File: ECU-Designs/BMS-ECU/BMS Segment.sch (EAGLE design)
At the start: 108 parts, among them Q1 P-CHANNEL_MOSFET_DMP3099L-7, Q10 P-CHANNEL_MOSFET_DMP3099L-7, Q11 P-CHANNEL_MOSFET_DMP3099L-7, Q12 P-CHANNEL_MOSFET_DMP3099L-7, Q13 NPN_BCP56T1, Q2 P-CHANNEL_MOSFET_DMP3099L-7, Q3 P-CHANNEL_MOSFET_DMP3099L-7, Q4 P-CHANNEL_MOSFET_DMP3099L-7, Q5 P-CHANNEL_MOSFET_DMP3099L-7, Q6 P-CHANNEL_MOSFET_DMP3099L-7, Q7 P-CHANNEL_MOSFET_DMP3099L-7, Q8 P-CHANNEL_MOSFET_DMP3099L-7, Q9 P-CHANNEL_MOSFET_DMP3099L-7

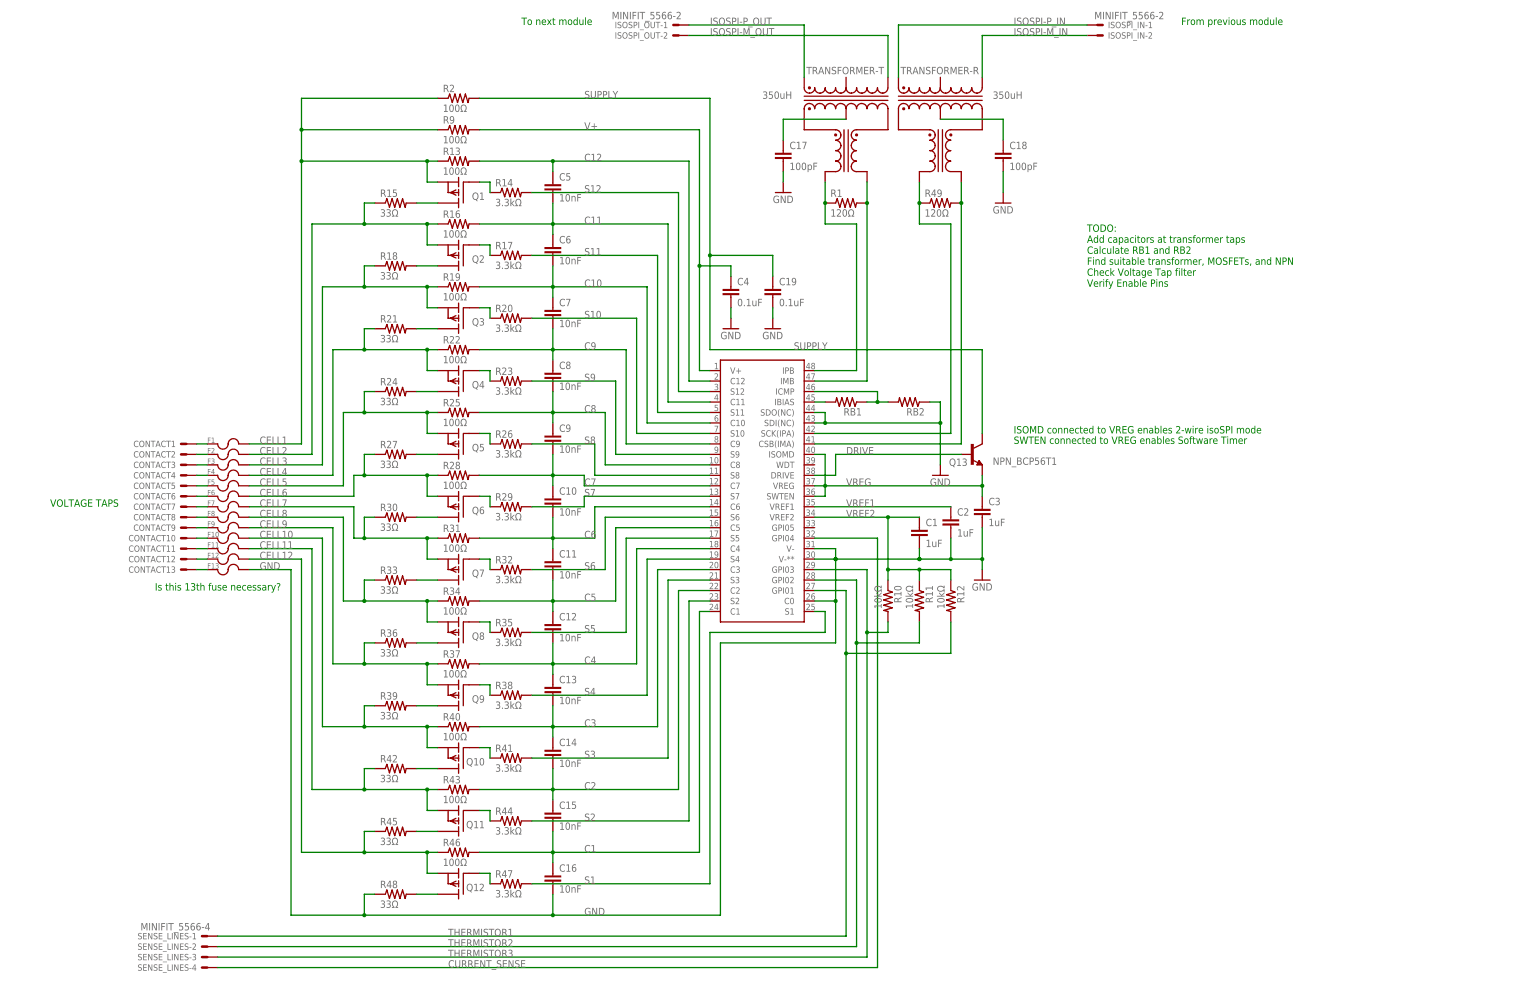
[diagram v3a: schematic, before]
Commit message: Update MC34161 name/desc, new 2016 vehicle pedal/dash controller board design, BSPD breakout test board
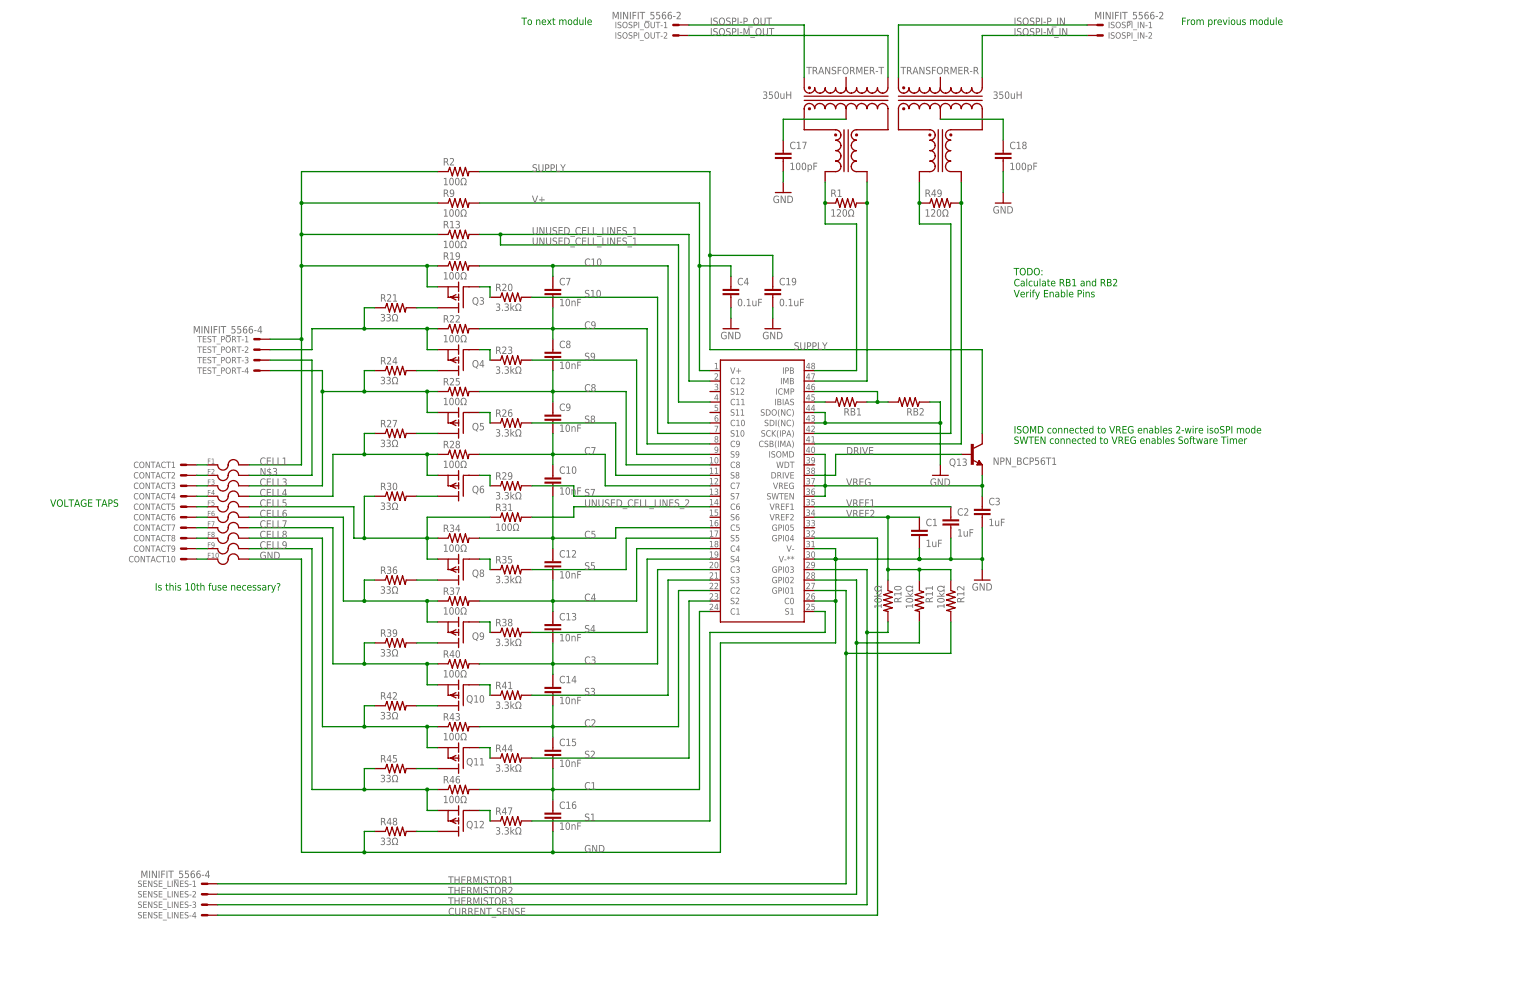
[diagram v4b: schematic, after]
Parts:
- removed C11, C5, C6: 10nF, HyTechDevices:CAP0805
- removed CONTACT11, CONTACT12, CONTACT13: SPRING_CONTACT, HyTechDevices:SPRING_CONTACT
- removed F11, F12, F13: C1Q_FUSE, HyTechDevices:C1Q_FUSE
- removed Q1, Q2, Q7: P-CHANNEL_MOSFET_DMP3099L-7, HyTechDevices:P-CHANNEL_MOSFET_DMP3099L-7
- removed R14, R17, R32: 3.3kΩ, HyTechDevices:RESISTOR0805-RES
- removed R15, R18, R33: 33Ω, HyTechDevices:RESISTOR2512
- removed R16: 100Ω, HyTechDevices:RESISTOR0805-RES
- added TEST_PORT: MINIFIT_5566-4, HyTechDevices:MINIFIT_5566-4
- F1, F10, F2, F3, F4, F5, F6, F7, F8, F9: value C1Q_FUSE -> 0751.0110_FUSE_CLIP; device HyTechDevices:C1Q_FUSE -> HyTechDevices:0751.0110_FUSE_CLIP
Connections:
- removed net C11: C5.2, C6.1, R16.2, U$2.C11
- removed net C12: C5.1, R13.2, U$2.C12
- removed net C6: C10.2, C11.1, R31.2, U$2.C6
- removed net CELL10: F10.2, Q10.S, R39.1, R40.1
- removed net CELL11: F11.2, Q11.S, R42.1, R43.1
- removed net CELL12: F12.2, Q12.S, R45.1, R46.1
- removed net N$10: Q1.G, R14.1
- removed net N$12: Q2.G, R17.1
- removed net N$13: Q2.D, R18.2
- removed net N$31 (its old number): CONTACT11.S, F11.1
- removed net N$32 (its old number): CONTACT12.S, F12.1
- removed net N$33 (its old number): CONTACT13.S, F13.1
- removed net N$38: Q7.D, R33.2
- removed net N$6: Q1.D, R15.2
- removed net N$71: Q7.G, R32.1
- removed net S11: R17.2, U$2.S11
- removed net S12: R14.2, U$2.S12
- removed net S6: R32.2, U$2.S6
- new net N$3: F2.2, TEST_PORT-3.S
- new net UNUSED_CELL_LINES_1: R13.2, U$2.C11, U$2.C12
- new net UNUSED_CELL_LINES_2: R31.2, U$2.C6
- net C10: no longer C6.2
- net C5: now also C10.2; no longer C11.2
- net CELL1: now also Q3.S, R19.1, TEST_PORT-1.S; no longer Q1.S
- net CELL2: now also Q4.S, R21.1, R22.1, TEST_PORT-2.S; no longer F2.2, Q2.S, R15.1, R16.1
- net CELL3: now also Q5.S, R24.1, R25.1, TEST_PORT-4.S; no longer Q3.S, R18.1, R19.1
- net CELL4: now also Q6.S, R27.1, R28.1; no longer Q4.S, R21.1, R22.1
- net CELL5: now also Q8.S, R30.1, R31.1, R34.1; no longer Q5.S, R24.1, R25.1
- net CELL6: now also Q9.S, R36.1, R37.1; no longer Q6.S, R27.1, R28.1
- net CELL7: now also Q10.S, R39.1, R40.1; no longer Q7.S, R30.1, R31.1
- net CELL8: now also Q11.S, R42.1, R43.1; no longer Q8.S, R33.1, R34.1
- net CELL9: now also Q12.S, R45.1, R46.1; no longer Q9.S, R36.1, R37.1
- net GND: now also F10.2; no longer F13.2
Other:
- note added: "Is this 10th fuse necessary?"
- note added: "TODO: Calculate RB1 and RB2 Verify Enable Pins"
- note removed: "Is this 13th fuse necessary?"
- note removed: "TODO: Add capacitors at transformer taps Calculate RB1 and RB2 Find suitable transformer, MOSFETs, and NPN Check Voltage Tap filter Verify Enable Pins"
- moved on the sheet: C10, C12, C13, C14, C15, C16, C7, C8, C9, CONTACT1, CONTACT10, CONTACT2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

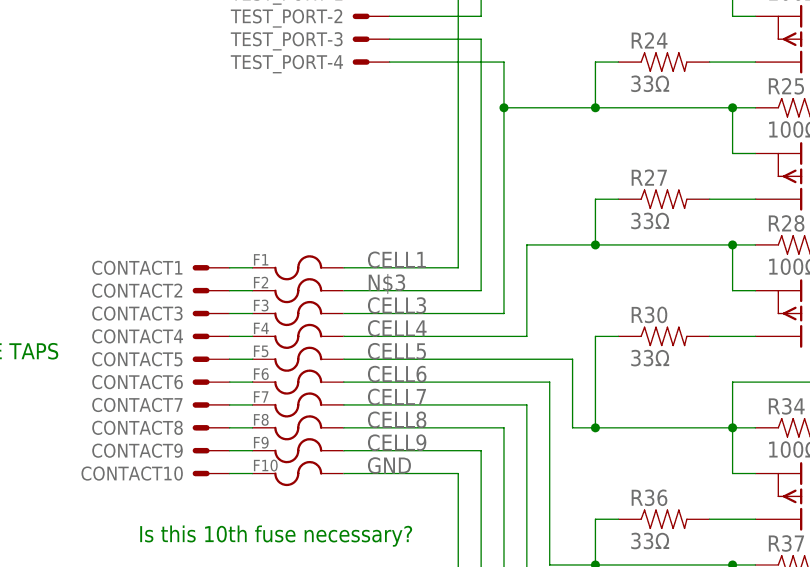
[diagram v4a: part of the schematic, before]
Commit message: Preliminary BMS Board Design Created
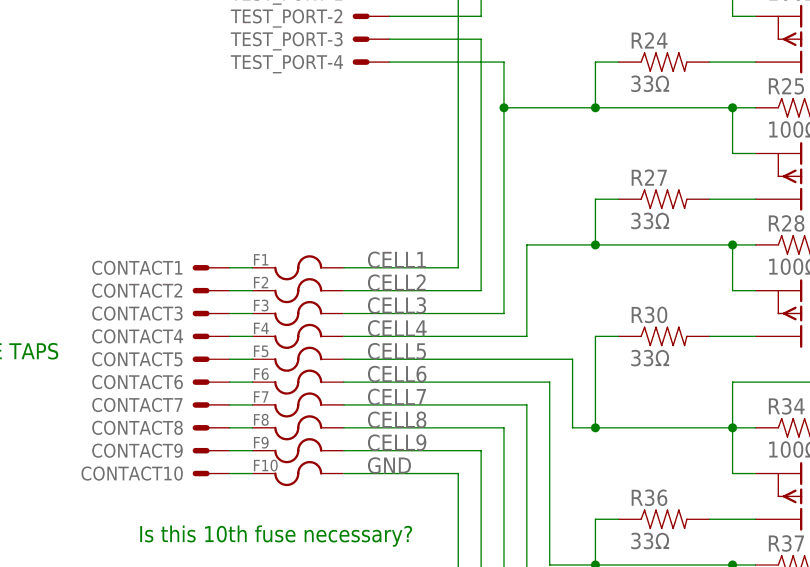
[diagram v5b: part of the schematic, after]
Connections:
- removed net N$3: F2.2, TEST_PORT-3.S
- net CELL2: now also F2.2, TEST_PORT-3.S
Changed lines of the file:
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@@
 <wire x1="-104.14" y1="66.04" x2="-104.14" y2="71.12" width="0.1524" layer="91"/>
+</segment>
+<segment>
+<pinref part="F2" gate="G$1" pin="2"/>
+<wire x1="-104.14" y1="35.56" x2="-119.38" y2="35.56" width="0.1524" layer="91"/>
+<label x="-116.84" y="35.56" size="1.778" layer="95"/>
+<wire x1="-104.14" y1="35.56" x2="-104.14" y2="63.5" width="0.1524" layer="91"/>
+<pinref part="TEST_PORT" gate="-3" pin="S"/>
+<wire x1="-114.3" y1="63.5" x2="-104.14" y2="63.5" width="0.1524" layer="91"/>
 </segment>
 </net>
@@
 </segment>
 </net>
-<net name="N$3" class="0">
-<segment>
-<pinref part="F2" gate="G$1" pin="2"/>
-<wire x1="-104.14" y1="35.56" x2="-119.38" y2="35.56" width="0.1524" layer="91"/>
-<label x="-116.84" y="35.56" size="1.778" layer="95"/>
-<wire x1="-104.14" y1="35.56" x2="-104.14" y2="63.5" width="0.1524" layer="91"/>
-<pinref part="TEST_PORT" gate="-3" pin="S"/>
-<wire x1="-114.3" y1="63.5" x2="-104.14" y2="63.5" width="0.1524" layer="91"/>
-</segment>
-</net>
